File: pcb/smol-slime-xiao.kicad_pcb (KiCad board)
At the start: 4 copper layers, 97.5 x 35.8 mm, 10 parts, among them U1 ICM-45686, U3 1532H, U4 XIAO-nRF52840-SMD

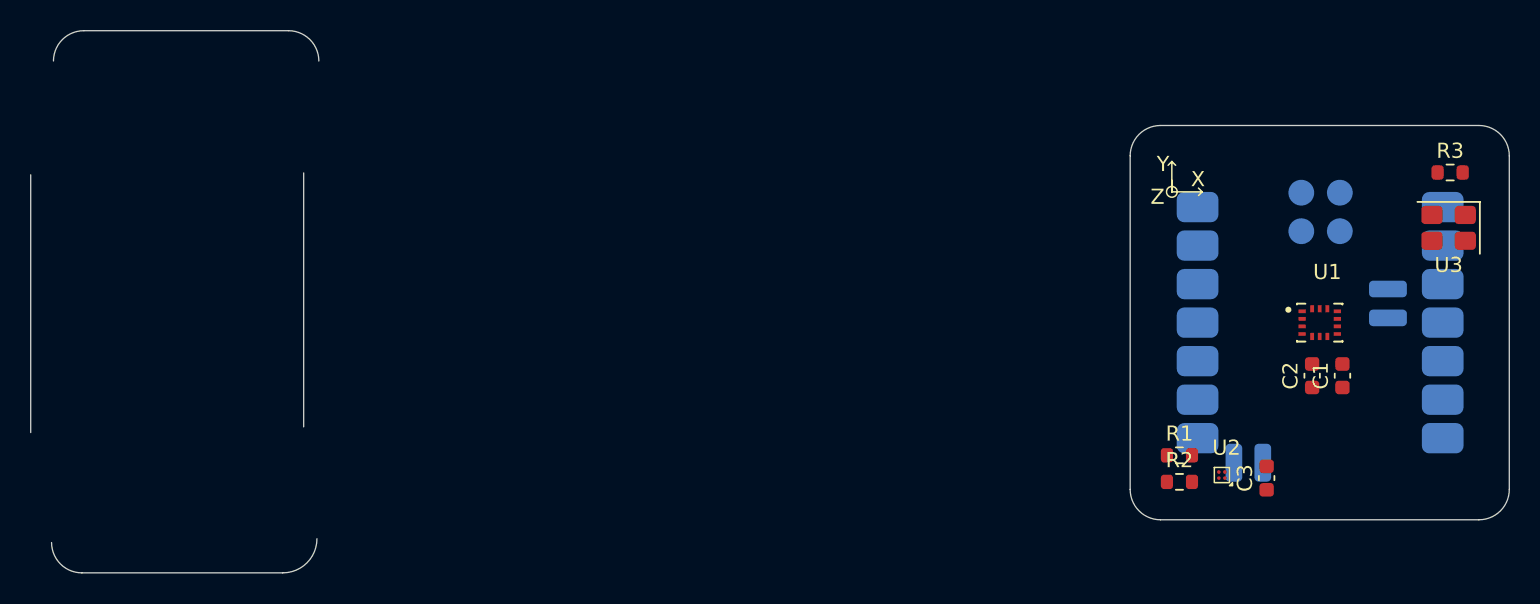
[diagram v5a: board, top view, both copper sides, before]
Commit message: Rework board shape and arrangement
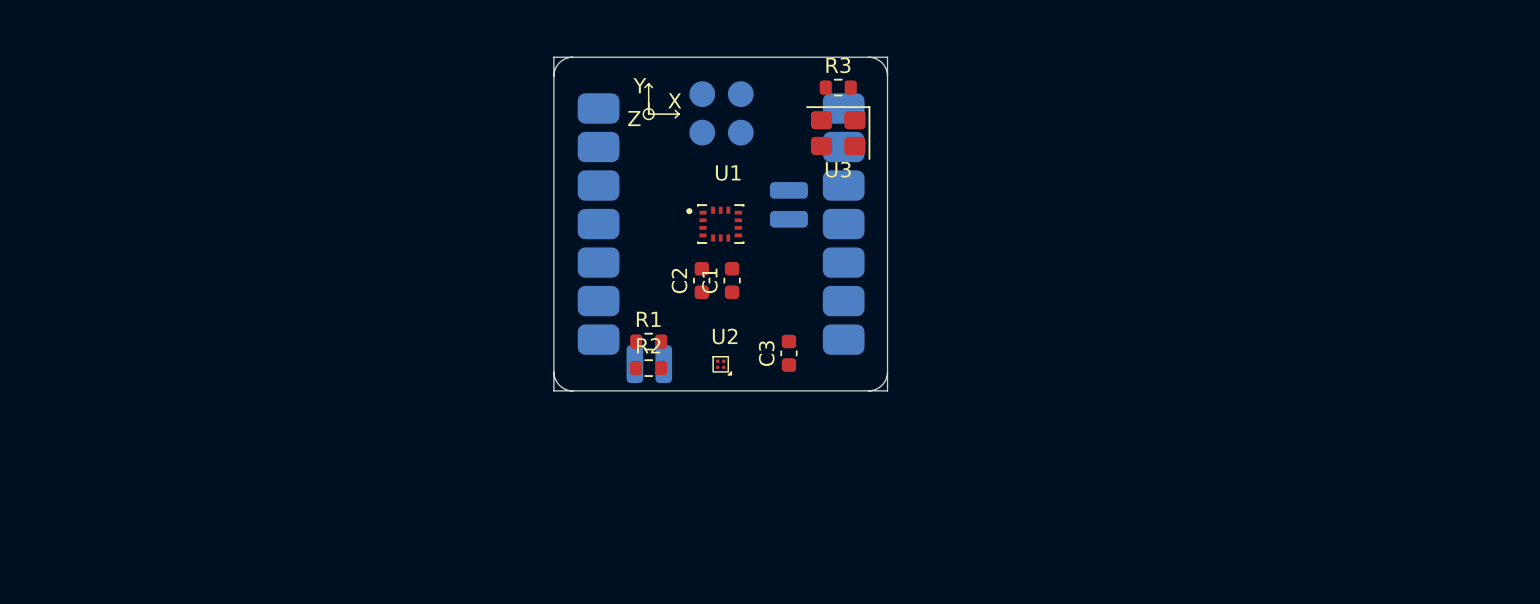
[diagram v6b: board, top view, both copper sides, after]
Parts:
- moved R3 40.7 mm to (157.8, 91.0)
- moved C1 40.7 mm to (150.8, 103.7)
- moved C2 40.7 mm to (148.8, 103.7)
- moved U3 40.7 mm to (157.8, 94.0)
- moved U1 40.0 mm to (150.0, 100.0)
- moved U4 40.0 mm to (150.0, 100.0)
- moved R1 35.8 mm to (145.2, 107.8)
- moved R2 35.8 mm to (145.2, 109.5)
- moved U2 33.8 mm to (150.0, 109.2)
- moved C3 32.6 mm to (154.5, 108.5)
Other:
- board size 97.5 x 35.8 mm -> 22 x 22 mm
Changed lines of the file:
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@@
 	(footprint "Resistor_SMD:R_0603_1608Metric"
 		(layer "F.Cu")
-		(at 198.1 96.6)
+		(at 157.75 91)
 		(descr "Resistor SMD 0603 (1608 Metric), square (rectangular) end terminal, IPC-7351 nominal, (Body size source: IPC-SM-782 page 72, https://www.pcb-3d.com/wordpress/wp-content/uploads/ipc-sm-782a_amendment_1_and_2.pdf), generated with kicad-footprint-generator")
 		(tags "resistor")
@@
 	(footprint "Resistor_SMD:R_0603_1608Metric"
 		(layer "F.Cu")
-		(at 180.25 117)
+		(at 145.25 109.5)
 		(descr "Resistor SMD 0603 (1608 Metric), square (rectangular) end terminal, IPC-7351 nominal, (Body size source: IPC-SM-782 page 72, https://www.pcb-3d.com/wordpress/wp-content/uploads/ipc-sm-782a_amendment_1_and_2.pdf), generated with kicad-footprint-generator")
 		(tags "resistor")
@@
 	(footprint "QMC6309:QMC6309"
 		(layer "F.Cu")
-		(at 183.05 116.55)
+		(at 150 109.25)
 		(property "Reference" "U2"
 			(at 0.3 -1.8 0)
@@
 	(footprint "Crystal:Crystal_SMD_3225-4Pin_3.2x2.5mm"
 		(layer "F.Cu")
-		(at 198 100.25 180)
+		(at 157.75 94 180)
 		(descr "SMD3225/4, Crystal, 3.2x2.5mm package, SMD, generated with kicad-footprint-generator make_crystal.py, http://www.txccrystal.com/images/pdf/7m-accuracy.pdf")
 		(property "Reference" "U3"
@@
 	(footprint "Capacitor_SMD:C_0603_1608Metric"
 		(layer "F.Cu")
-		(at 186 116.75 90)
+		(at 154.5 108.525 90)
 		(descr "Capacitor SMD 0603 (1608 Metric), square (rectangular) end terminal, IPC-7351 nominal, (Body size source: IPC-SM-782 page 76, https://www.pcb-3d.com/wordpress/wp-content/uploads/ipc-sm-782a_amendment_1_and_2.pdf), generated with kicad-footprint-generator")
 		(tags "capacitor")
@@
 	(footprint "Resistor_SMD:R_0603_1608Metric"
 		(layer "F.Cu")
-		(at 180.25 115.25)
+		(at 145.25 107.75)
 		(descr "Resistor SMD 0603 (1608 Metric), square (rectangular) end terminal, IPC-7351 nominal, (Body size source: IPC-SM-782 page 72, https://www.pcb-3d.com/wordpress/wp-content/uploads/ipc-sm-782a_amendment_1_and_2.pdf), generated with kicad-footprint-generator")
 		(tags "resistor")
@@
 	(footprint "Capacitor_SMD:C_0603_1608Metric"
 		(layer "F.Cu")
-		(at 191 110 90)
+		(at 150.75 103.725 90)
 		(descr "Capacitor SMD 0603 (1608 Metric), square (rectangular) end terminal, IPC-7351 nominal, (Body size source: IPC-SM-782 page 76, https://www.pcb-3d.com/wordpress/wp-content/uploads/ipc-sm-782a_amendment_1_and_2.pdf), generated with kicad-footprint-generator")
 		(tags "capacitor")
@@
 	(footprint "Capacitor_SMD:C_0603_1608Metric"
 		(layer "F.Cu")
-		(at 189 110 90)
+		(at 148.75 103.725 90)
 		(descr "Capacitor SMD 0603 (1608 Metric), square (rectangular) end terminal, IPC-7351 nominal, (Body size source: IPC-SM-782 page 76, https://www.pcb-3d.com/wordpress/wp-content/uploads/ipc-sm-782a_amendment_1_and_2.pdf), generated with kicad-footprint-generator")
 		(tags "capacitor")
@@
 	(footprint "ICM-45686:IC_ICM-45686"
 		(layer "F.Cu")
-		(at 189.5 106.5)
+		(at 150 100)
 		(property "Reference" "U1"
 			(at 0.5 -3.3375 0)
@@
 		)
 		(property "Value" "ICM-45686"
-			(at 14.25 -0.9625 0)
+			(at 6.75 0 0)
 			(layer "F.Fab")
 			(effects
@@
 			(polygon
 				(pts
-					(xy 188.6 105.85) (xy 190.4 105.85) (xy 190.4 107.15) (xy 188.6 107.15)
+					(xy 149.1 99.35) (xy 150.9 99.35) (xy 150.9 100.65) (xy 149.1 100.65)
 				)
 			)
@@
 			(polygon
 				(pts
-					(xy 188.6 105.85) (xy 190.4 105.85) (xy 190.4 107.15) (xy 188.6 107.15)
+					(xy 149.1 99.35) (xy 150.9 99.35) (xy 150.9 100.65) (xy 149.1 100.65)
 				)
 			)
@@
 	(footprint "Seeed Studio XIAO Series Library:XIAO-nRF52840-SMD"
 		(layer "B.Cu")
-		(at 189.5 106.5 180)
+		(at 150 100 180)
 		(property "Reference" "U4"
 			(at -9.445 11.5 0)
@@
 	)
 	(gr_line
-		(start 179.75 97.125)
-		(end 179.75 97.875)
+		(start 145.25 92)
+		(end 145.25 92.75)
 		(stroke
 			(width 0.1)
@@
 	)
 	(gr_line
-		(start 181.75 97.875)
-		(end 179.75 97.875)
+		(start 147.25 92.75)
+		(end 145.25 92.75)
 		(stroke
 			(width 0.1)
@@
 	)
 	(gr_line
-		(start 181.75 97.875)
-		(end 181.5 97.625)
+		(start 147.25 92.75)
+		(end 147 92.5)
 		(stroke
 			(width 0.1)
@@
 	)
 	(gr_circle
-		(center 179.75 97.875)
-		(end 180 97.625)
+		(center 145.25 92.75)
+		(end 145.5 92.5)
 		(stroke
 			(width 0.1)
@@
 	)
 	(gr_line
-		(start 179.75 97.875)
-		(end 179.75 95.875)
+		(start 145.25 92.75)
+		(end 145.25 90.75)
 		(stroke
 			(width 0.1)
@@
 	)
 	(gr_line
-		(start 181.75 97.875)
-		(end 181.5 98.125)
+		(start 147.25 92.75)
+		(end 147 93)
 		(stroke
 			(width 0.1)
@@
 	)
 	(gr_line
-		(start 179.75 95.875)
-		(end 179.5 96.125)
+		(start 145.25 90.75)
+		(end 145 91)
 		(stroke
 			(width 0.1)
@@
 	)
 	(gr_line
-		(start 179.75 95.875)
-		(end 180 96.125)
+		(start 145.25 90.75)
+		(end 145.5 91)
 		(stroke
 			(width 0.1)
@@
 	)
 	(gr_arc
-		(start 202 117.5)
-		(mid 201.414214 118.914214)
-		(end 200 119.5)
+		(start 139 90.25)
+		(mid 139.366117 89.366117)
+		(end 140.25 89)
 		(stroke
 			(width 0.05)
@@
 	)
 	(gr_arc
-		(start 123.375 120.75)
-		(mid 122.71599 122.34099)
-		(end 121.125 123)
+		(start 159.75 89)
+		(mid 160.633883 89.366117)
+		(end 161 90.25)
 		(stroke
 			(width 0.05)
@@
 		(layer "Edge.Cuts")
 	)
-	(gr_line
-		(start 202 95.5)
-		(end 202 117.5)
+	(gr_arc
+		(start 161 109.75)
+		(mid 160.633883 110.633883)
+		(end 159.75 111)
 		(stroke
 			(width 0.05)
@@
 		(layer "Edge.Cuts")
 	)
-	(gr_line
-		(start 177 95.5)
-		(end 177 117.5)
+	(gr_rect
+		(start 139 89)
+		(end 161 111)
+		(stroke
+			(width 0.05)
+			(type solid)
+		)
+		(fill no)
+		(layer "Edge.Cuts")
+	)
+	(gr_arc
+		(start 140.25 111)
+		(mid 139.366117 110.633883)
+		(end 139 109.75)
 		(stroke
 			(width 0.05)
@@
 		(layer "Edge.Cuts")
 	)
-	(gr_arc
-		(start 106 89.25)
-		(mid 106.585786 87.835786)
-		(end 108 87.25)
-		(stroke
-			(width 0.05)
-			(type default)
-		)
-		(layer "Edge.Cuts")
-	)
-	(gr_line
-		(start 107.875 123)
-		(end 121.125 123)
-		(stroke
-			(width 0.05)
-			(type default)
-		)
-		(layer "Edge.Cuts")
-	)
-	(gr_arc
-		(start 177 95.5)
-		(mid 177.585786 94.085786)
-		(end 179 93.5)
-		(stroke
-			(width 0.05)
-			(type default)
-		)
-		(layer "Edge.Cuts")
-	)
-	(gr_arc
-		(start 179 119.5)
-		(mid 177.585786 118.914214)
-		(end 177 117.5)
-		(stroke
-			(width 0.05)
-			(type default)
-		)
-		(layer "Edge.Cuts")
-	)
-	(gr_line
-		(start 104.5 96.75)
-		(end 104.5 113.75)
-		(stroke
-			(width 0.05)
-			(type default)
-		)
-		(layer "Edge.Cuts")
-	)
-	(gr_arc
-		(start 121.5 87.25)
-		(mid 122.914214 87.835786)
-		(end 123.5 89.25)
-		(stroke
-			(width 0.05)
-			(type default)
-		)
-		(layer "Edge.Cuts")
-	)
-	(gr_line
-		(start 122.5 113.375)
-		(end 122.5 96.625)
-		(stroke
-			(width 0.05)
-			(type default)
-		)
-		(layer "Edge.Cuts")
-	)
-	(gr_arc
-		(start 200 93.5)
-		(mid 201.414214 94.085786)
-		(end 202 95.5)
-		(stroke
-			(width 0.05)
-			(type default)
-		)
-		(layer "Edge.Cuts")
-	)
-	(gr_line
-		(start 200 119.5)
-		(end 179 119.5)
-		(stroke
-			(width 0.05)
-			(type default)
-		)
-		(layer "Edge.Cuts")
-	)
-	(gr_line
-		(start 121.5 87.25)
-		(end 108 87.25)
-		(stroke
-			(width 0.05)
-			(type default)
-		)
-		(layer "Edge.Cuts")
-	)
-	(gr_line
-		(start 200 93.5)
-		(end 179 93.5)
-		(stroke
-			(width 0.05)
-			(type default)
-		)
-		(layer "Edge.Cuts")
-	)
-	(gr_arc
-		(start 107.875 123)
-		(mid 106.460786 122.414214)
-		(end 105.875 121)
-		(stroke
-			(width 0.05)
-			(type default)
-		)
-		(layer "Edge.Cuts")
-	)
 	(gr_text "X"
-		(at 181 97.625 0)
+		(at 146.5 92.5 0)
 		(layer "F.SilkS")
 		(effects
@@
 	)
 	(gr_text "Z"
-		(at 178.335787 98.789214 0)
+		(at 143.835787 93.664214 0)
 		(layer "F.SilkS")
 		(effects
@@
 	)
 	(gr_text "Y"
-		(at 178.75 96.625 0)
+		(at 144.25 91.5 0)
 		(layer "F.SilkS")
 		(effects

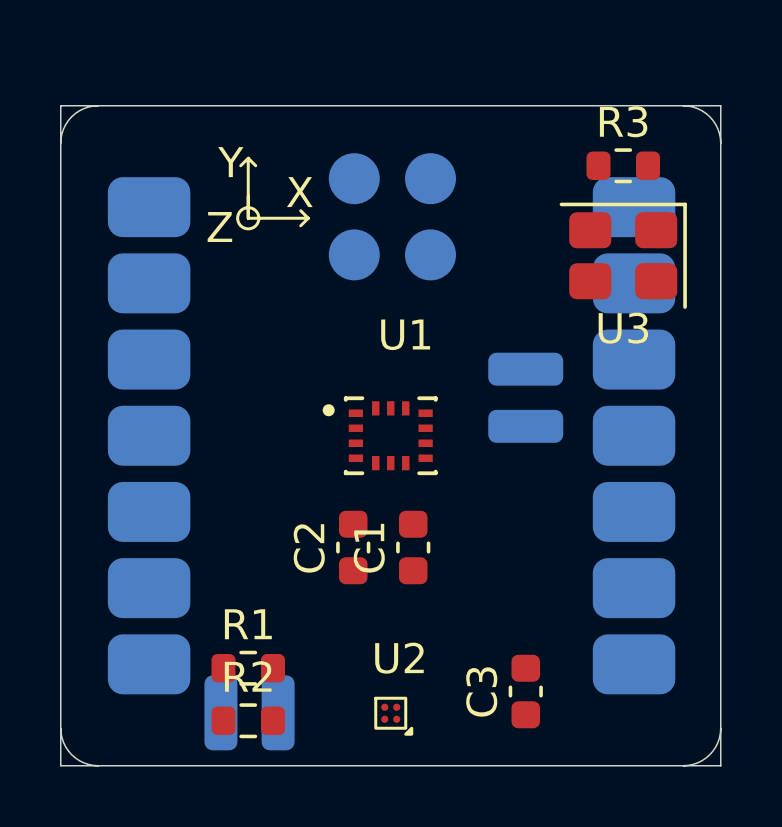
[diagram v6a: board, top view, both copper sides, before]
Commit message: Update edge-cuts for board
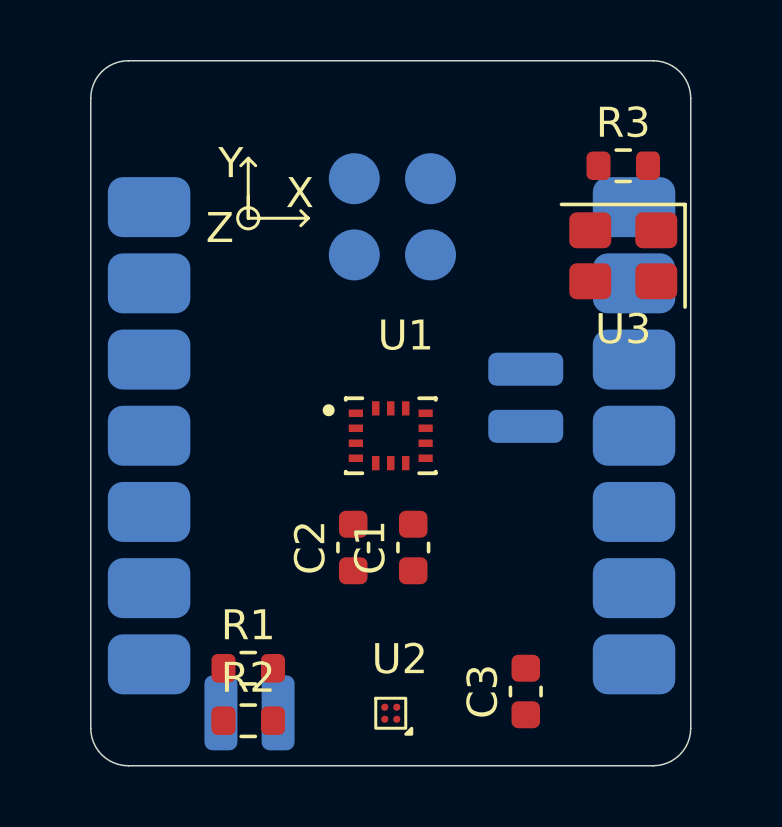
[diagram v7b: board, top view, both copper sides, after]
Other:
- board size 22 x 22 mm -> 20 x 23.5 mm
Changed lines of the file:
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@@
 		(layer "F.SilkS")
 	)
-	(gr_arc
-		(start 139 90.25)
-		(mid 139.366117 89.366117)
-		(end 140.25 89)
+	(gr_line
+		(start 140 88.75)
+		(end 140 109.75)
 		(stroke
 			(width 0.05)
@@
 	)
 	(gr_arc
-		(start 159.75 89)
-		(mid 160.633883 89.366117)
-		(end 161 90.25)
+		(start 140 88.75)
+		(mid 140.366117 87.866117)
+		(end 141.25 87.5)
+		(stroke
+			(width 0.05)
+			(type default)
+		)
+		(layer "Edge.Cuts")
+	)
+	(gr_line
+		(start 141.25 111)
+		(end 158.75 111)
 		(stroke
 			(width 0.05)
@@
 	)
 	(gr_arc
-		(start 161 109.75)
-		(mid 160.633883 110.633883)
-		(end 159.75 111)
+		(start 158.75 87.5)
+		(mid 159.633883 87.866117)
+		(end 160 88.75)
 		(stroke
 			(width 0.05)
@@
 		(layer "Edge.Cuts")
 	)
-	(gr_rect
-		(start 139 89)
-		(end 161 111)
+	(gr_arc
+		(start 160 109.75)
+		(mid 159.633883 110.633883)
+		(end 158.75 111)
 		(stroke
 			(width 0.05)
-			(type solid)
+			(type default)
 		)
-		(fill no)
+		(layer "Edge.Cuts")
+	)
+	(gr_line
+		(start 160 109.75)
+		(end 160 88.75)
+		(stroke
+			(width 0.05)
+			(type default)
+		)
 		(layer "Edge.Cuts")
 	)
 	(gr_arc
-		(start 140.25 111)
-		(mid 139.366117 110.633883)
-		(end 139 109.75)
+		(start 141.25 111)
+		(mid 140.366117 110.633883)
+		(end 140 109.75)
 		(stroke
 			(width 0.05)
+			(type default)
+		)
+		(layer "Edge.Cuts")
+	)
+	(gr_line
+		(start 158.75 87.5)
+		(end 141.25 87.5)
+		(stroke
+			(width 0.05)

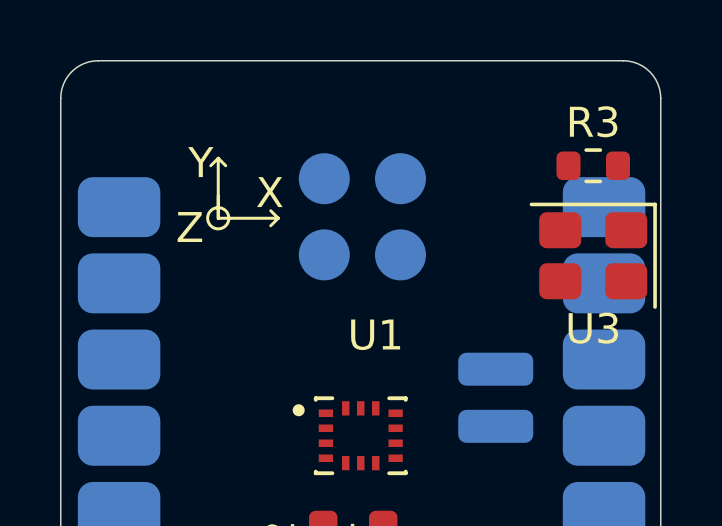
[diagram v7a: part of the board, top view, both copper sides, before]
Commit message: Added power pads to board
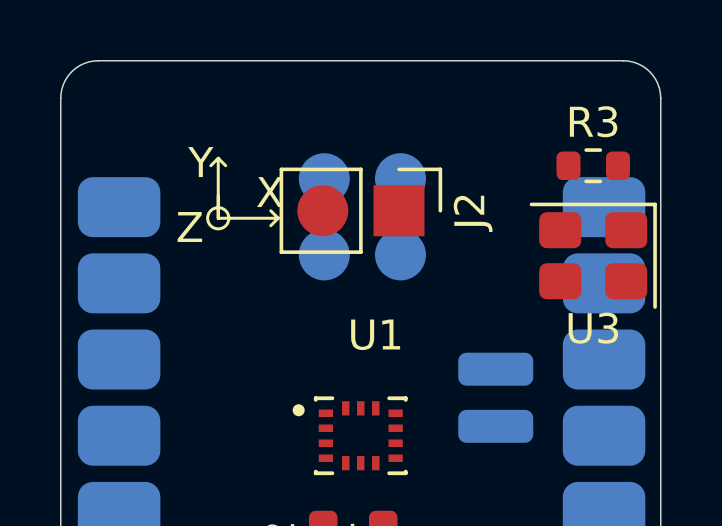
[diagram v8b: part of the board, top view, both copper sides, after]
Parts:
- added J2: Conn_01x02, Generic:PinPads_1x02_P2.54mm, F.Cu at (151.3, 92.5)
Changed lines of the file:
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@@
 			)
 		)
-		(property "Datasheet" ""
+		(property "Datasheet" "~"
 			(at 0 0 0)
 			(layer "F.Fab")
@@
 			)
 		)
-		(property "Datasheet" ""
+		(property "Datasheet" "~"
 			(at 0 0 0)
 			(layer "F.Fab")
@@
 			)
 		)
-		(property "Datasheet" ""
+		(property "Datasheet" "~"
 			(at 0 0 90)
 			(layer "F.Fab")
@@
 			)
 		)
-		(property "Datasheet" ""
+		(property "Datasheet" "~"
 			(at 0 0 0)
 			(layer "F.Fab")
@@
 		(embedded_fonts no)
 		(model "${KICAD9_3DMODEL_DIR}/Resistor_SMD.3dshapes/R_0603_1608Metric.step"
+			(offset
+				(xyz 0 0 0)
+			)
+			(scale
+				(xyz 1 1 1)
+			)
+			(rotate
+				(xyz 0 0 0)
+			)
+		)
+	)
+	(footprint "Generic:PinPads_1x02_P2.54mm"
+		(layer "F.Cu")
+		(at 151.275 92.5 -90)
+		(descr "Through hole straight pin header, 1x02, 2.54mm pitch, single row")
+		(tags "Through hole pin header THT 1x02 2.54mm single row")
+		(property "Reference" "J2"
+			(at 0 -2.38 90)
+			(layer "F.SilkS")
+			(effects
+				(font
+					(size 1 1)
+					(thickness 0.15)
+				)
+			)
+		)
+		(property "Value" "Conn_01x02"
+			(at 0 4.92 90)
+			(layer "F.Fab")
+			(effects
+				(font
+					(size 1 1)
+					(thickness 0.15)
+				)
+			)
+		)
+		(property "Datasheet" "~"
+			(at 0 0 90)
+			(layer "F.Fab")
+			(hide yes)
+			(effects
+				(font
+					(size 1.27 1.27)
+					(thickness 0.15)
+				)
+			)
+		)
+		(property "Description" "Generic connector, single row, 01x02, script generated (kicad-library-utils/schlib/autogen/connector/)"
+			(at 0 0 90)
+			(layer "F.Fab")
+			(hide yes)
+			(effects
+				(font
+					(size 1.27 1.27)
+					(thickness 0.15)
+				)
+			)
+		)
+		(property ki_fp_filters "Connector*:*_1x??_*")
+		(sheetname "/")
+		(sheetfile "smol-slime-xiao.kicad_sch")
+		(attr through_hole)
+		(fp_line
+			(start -1.38 3.92)
+			(end 1.38 3.92)
+			(stroke
+				(width 0.12)
+				(type solid)
+			)
+			(layer "F.SilkS")
+		)
+		(fp_line
+			(start -1.38 1.27)
+			(end -1.38 3.92)
+			(stroke
+				(width 0.12)
+				(type solid)
+			)
+			(layer "F.SilkS")
+		)
+		(fp_line
+			(start -1.38 1.27)
+			(end 1.38 1.27)
+			(stroke
+				(width 0.12)
+				(type solid)
+			)
+			(layer "F.SilkS")
+		)
+		(fp_line
+			(start 1.38 1.27)
+			(end 1.38 3.92)
+			(stroke
+				(width 0.12)
+				(type solid)
+			)
+			(layer "F.SilkS")
+		)
+		(fp_line
+			(start -1.38 0)
+			(end -1.38 -1.38)
+			(stroke
+				(width 0.12)
+				(type solid)
+			)
+			(layer "F.SilkS")
+		)
+		(fp_line
+			(start -1.38 -1.38)
+			(end 0 -1.38)
+			(stroke
+				(width 0.12)
+				(type solid)
+			)
+			(layer "F.SilkS")
+		)
+		(fp_line
+			(start -1.77 4.32)
+			(end 1.77 4.32)
+			(stroke
+				(width 0.05)
+				(type solid)
+			)
+			(layer "F.CrtYd")
+		)
+		(fp_line
+			(start 1.77 4.32)
+			(end 1.77 -1.77)
+			(stroke
+				(width 0.05)
+				(type solid)
+			)
+			(layer "F.CrtYd")
+		)
+		(fp_line
+			(start -1.77 -1.77)
+			(end -1.77 4.32)
+			(stroke
+				(width 0.05)
+				(type solid)
+			)
+			(layer "F.CrtYd")
+		)
+		(fp_line
+			(start 1.77 -1.77)
+			(end -1.77 -1.77)
+			(stroke
+				(width 0.05)
+				(type solid)
+			)
+			(layer "F.CrtYd")
+		)
+		(fp_line
+			(start -1.27 3.81)
+			(end -1.27 -0.635)
+			(stroke
+				(width 0.1)
+				(type solid)
+			)
+			(layer "F.Fab")
+		)
+		(fp_line
+			(start 1.27 3.81)
+			(end -1.27 3.81)
+			(stroke
+				(width 0.1)
+				(type solid)
+			)
+			(layer "F.Fab")
+		)
+		(fp_line
+			(start -1.27 -0.635)
+			(end -0.635 -1.27)
+			(stroke
+				(width 0.1)
+				(type solid)
+			)
+			(layer "F.Fab")
+		)
+		(fp_line
+			(start -0.635 -1.27)
+			(end 1.27 -1.27)
+			(stroke
+				(width 0.1)
+				(type solid)
+			)
+			(layer "F.Fab")
+		)
+		(fp_line
+			(start 1.27 -1.27)
+			(end 1.27 3.81)
+			(stroke
+				(width 0.1)
+				(type solid)
+			)
+			(layer "F.Fab")
+		)
+		(fp_text user "${REFERENCE}"
+			(at 0 1.27 0)
+			(layer "F.Fab")
+			(effects
+				(font
+					(size 1 1)
+					(thickness 0.15)
+				)
+			)
+		)
+		(pad "1" smd rect
+			(at 0 0 270)
+			(size 1.7 1.7)
+			(layers "F.Cu" "F.Mask" "F.Paste")
+			(net 1 "GND")
+			(pinfunction "Pin_1")
+			(pintype "passive")
+		)
+		(pad "2" smd circle
+			(at 0 2.54 270)
+			(size 1.7 1.7)
+			(layers "F.Cu" "F.Mask" "F.Paste")
+			(net 18 "+5V")
+			(pinfunction "Pin_2")
+			(pintype "passive")
+		)
+		(embedded_fonts no)
+		(model "${KICAD9_3DMODEL_DIR}/Connector_PinHeader_2.54mm.3dshapes/PinHeader_1x02_P2.54mm_Vertical.step"
 			(offset
 				(xyz 0 0 0)
@@
 			)
 		)
-		(property "Datasheet" ""
+		(property "Datasheet" "~"
 			(at 0 0 90)
 			(layer "F.Fab")
@@
 			)
 		)
-		(property "Datasheet" ""
+		(property "Datasheet" "~"
 			(at 0 0 90)
 			(layer "F.Fab")
@@
 		)
 		(property "Value" "ICM-45686"
-			(at 6.75 0 0)
-			(layer "F.Fab")
-			(effects
+			(at 14.5 -0.25 0)
+			(layer "F.Fab")
+			(effects
